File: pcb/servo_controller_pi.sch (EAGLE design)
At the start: 70 parts, among them IC1 PIC18F452, IC2 LM2936MP-5.0, IC3 MAX4173FESA+, IC4 LM2936MP-3.3, IC5 4512D, Q1 10Mhz, Q2 BUZ10

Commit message: Raspberry Pi pcb version
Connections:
- net +3V3: now also C10.1, C11.1, C3.1, C6.1, EXT.1, GY-27.5, IC1.VDD, IC1.VDD@1, IC3.VCC, IC5P.VDD, LED-STRIP.4, R5.2, R6.2, R7.2, SV1.1, SV1.3, SV1.5, SV1.7, SV2.1, SV2.3, SV2.5, SV2.7, VDD.TP; no longer U$3.17-DNC
- net +5V: no longer C10.1, C11.1, C3.1, C6.1, EXT.1, GY-27.5, IC1.VDD, IC1.VDD@1, IC3.VCC, IC5P.VDD, LED-STRIP.4, R5.2, R6.2, R7.2, SV1.1, SV1.3, SV1.5, SV1.7, SV2.1, SV2.3, SV2.5, SV2.7, U$3.4-DNC, VDD.TP
- net LIPO_VOLTAGE: now also IC1.RA5/AN4
- net SERVO_CURRENT: now also IC1.RE0/!RD/AN5
- net VSS: no longer U$3.14-DNC, U$3.20-DNC, U$3.25-DNC, U$3.9-DNC
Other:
- note added: "Sensors"
- moved on the sheet: C10, C7, C8, D4, IC5, IC5P, Q1, RN1, SV1, SV2

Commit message: Schema Pi
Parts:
- removed EXT: (no value), con-lstb:MA03-2
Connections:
- removed net N$16: SJ1.2
- removed net OPTION0: EXT.3
- removed net OPTION1: EXT.5
- removed net OPTION2: EXT.6
- removed net OPTION3: EXT.4
- removed net RX_FROM_ARDUINO: IC1.TX/RC6
- removed net SWITCH0: R6.1, S0.S
- removed net SWITCH1: R5.1, S1.S1
- removed net TX_FROM_ARDUINO: IC1.RX/RC7
- new net RX_PI: IC1.TX/RC6, U$3.10-RX
- new net SO: U$3.23-SPI-SCLK
- new net SW0: R6.1, S0.S, U$3.16-GPIO4
- new net SW1: R5.1, S1.S1, U$3.18-GPIO5
- new net TX_PI: IC1.RX/RC7, U$3.8-TX
- net +3V3: no longer EXT.1, LED-STRIP.4
- net +5V: now also LED-STRIP.4
- net ADDRA: now also U$3.22-GPIO6
- net ADDRB: now also U$3.24-SPI-CE0-N
- net ADDRC: now also U$3.26-SPI-CE1-N
- net DO: now also U$3.19-SPI-MOSI
- net LED0: now also U$3.7-GPIO7
- net LED1: now also U$3.11-GPIO0
- net OUT: now also U$3.12-GPIO1
- net POUT: now also U$3.15-GPIO3
- net SCL: now also U$3.5-SCL0
- net SDA: now also U$3.3-SDA0
- net VSS: no longer EXT.2
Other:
- moved on the sheet: C11, C3, D2, GY-27, IC3, IN-1, IN-2, LED-STRIP, OUT-1, OUT-2, Q2, R5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

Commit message: Raspberry Pi PCB
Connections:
- net UC_RESET: no longer SJ1.1
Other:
- moved on the sheet: SJ1
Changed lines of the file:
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@@
 <instance part="VSS25" gate="G$1" x="38.1" y="200.66"/>
 <instance part="VSS26" gate="G$1" x="157.48" y="180.34"/>
-<instance part="SJ1" gate="1" x="332.74" y="121.92" rot="R90"/>
+<instance part="SJ1" gate="1" x="180.34" y="132.08" rot="R90"/>
 <instance part="C9" gate="G$1" x="86.36" y="220.98"/>
 <instance part="VSS27" gate="G$1" x="86.36" y="200.66"/>
@@
 <pinref part="RESET" gate="G$1" pin="TP"/>
 </segment>
-<segment>
-<pinref part="SJ1" gate="1" pin="1"/>
-<wire x1="332.74" y1="116.84" x2="332.74" y2="114.3" width="0.1524" layer="91"/>
-<junction x="332.74" y="114.3"/>
-<label x="327.66" y="116.84" size="1.778" layer="95"/>
-</segment>
-</net>
+</net>

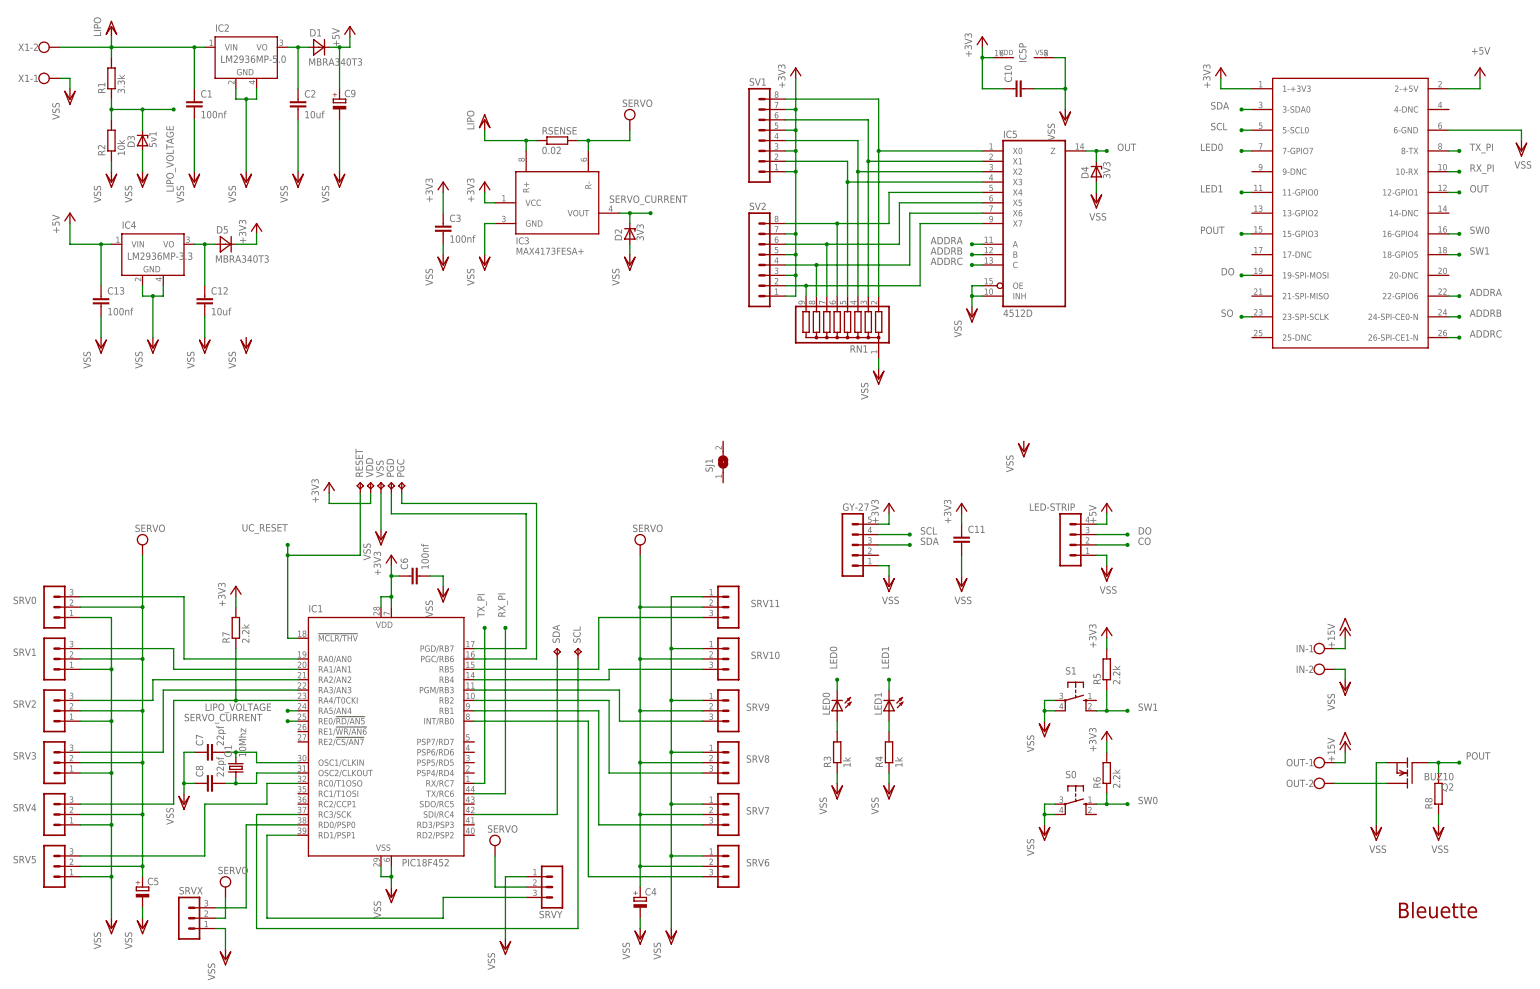
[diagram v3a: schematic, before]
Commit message: Sensor board milling + Raspberry Pi update
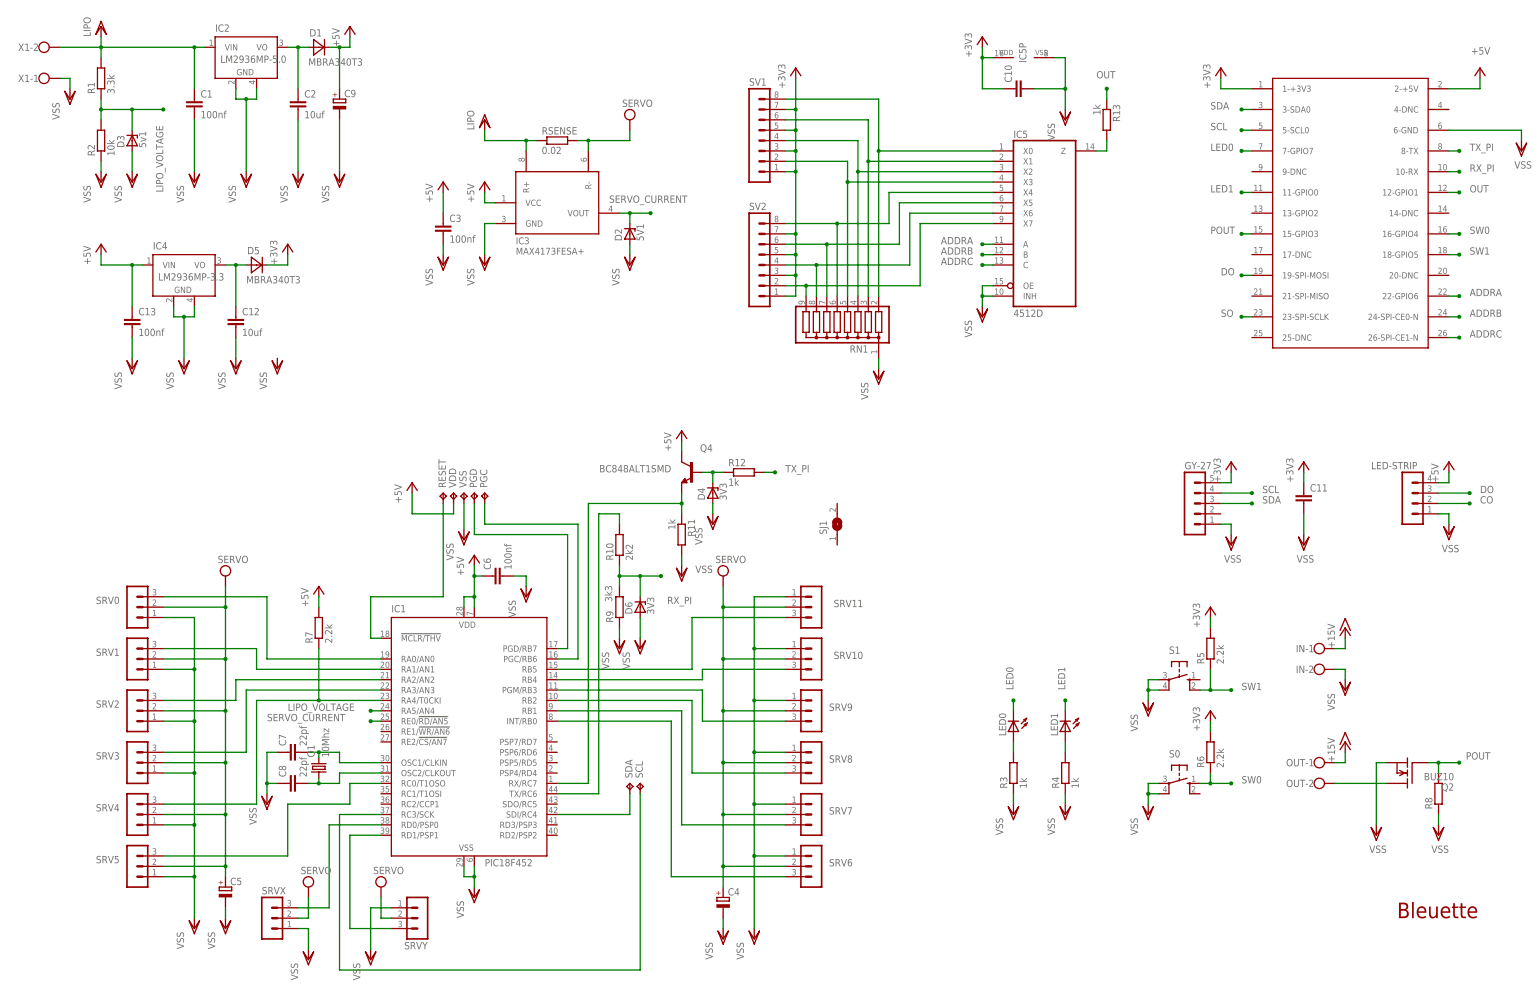
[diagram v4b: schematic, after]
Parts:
- added D6: 3V3, diode:ZENER-DIODESOT23
- added Q4: BC848ALT1SMD, transistor-npn:BC848ALT1SMD
- added R10: 2k2, rcl:R-EU_M0805
- added R11, R12, R13: 1k, rcl:R-EU_M0805
- added R9: 3k3, rcl:R-EU_M0805
- D2: value 3V3 -> 5V1
- R1, R2: device rcl:R-EU_M1206 -> rcl:R-EU_M0805
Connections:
- new net N$15: IC1.RX/RC7, Q4.E, R11.1
- new net N$16: IC1.TX/RC6, R10.2
- new net N$21: D4.C, Q4.B, R12.1
- new net N$37: IC5A.Z, R13.2
- net +3V3: no longer C3.1, C6.1, IC1.VDD, IC1.VDD@1, IC3.VCC, R7.2, VDD.TP
- net +5V: now also C3.1, C6.1, IC1.VDD, IC1.VDD@1, IC3.VCC, Q4.C, R7.2, VDD.TP
- net OUT: now also R13.1; no longer D4.C, IC5A.Z
- net RX_PI: now also D6.C, R10.1, R9.2; no longer IC1.TX/RC6
- net TX_PI: now also R12.2; no longer IC1.RX/RC7
- net VSS: now also D6.A, R11.2, R9.1
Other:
- moved on the sheet: C11, C12, C13, C4, C5, C6, C7, C8, D3, D4, D5, GY-27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

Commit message: RaspPi Board
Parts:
- added IC7: LM358D, linear:LM358D
- C3, C6, C7, C8: device rcl:C-EUC1206 -> rcl:C-EUC0805
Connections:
- net +5V: no longer U$3.2-+5V
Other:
- moved on the sheet: C3, C6, D2, IC3, RSENSE

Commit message: Rapsberry Pi board
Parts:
- removed D4: 3V3, diode:ZENER-DIODESOT23
- removed GY-27: (no value), con-lstb:MA05-1
- removed LED0, LED1: (no value), led:LEDCHIPLED_0805
- removed R3, R4: 1k, rcl:R-EU_M0805
- removed R5, R6: 2.2k, rcl:R-EU_M0805
- removed S0, S1: (no value), switch-omron:10-XX
- added LED2: (no value), led:LEDCHIPLED_0805
- added R14: 1k, rcl:R-EU_M0805
- added SV3: (no value), con-lstb:MA04-2
- added U$4: GY-27, gy-27:GY-27
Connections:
- net DO renamed DI
- removed net CO: LED-STRIP.2
- removed net LED0: LED0.C, U$3.7-GPIO7
- removed net LED1: LED1.C, U$3.11-GPIO0
- removed net N$7: LED0.A, R3.2
- removed net N$8: LED1.A, R4.2
- removed net SO: U$3.23-SPI-SCLK
- removed net SW0: R6.1, S0.S, U$3.16-GPIO4
- removed net SW1: R5.1, S1.S1, U$3.18-GPIO5
- new net N$39: LED2.A, R14.2
- new net OPTION0: SV3.3, U$3.7-GPIO7
- new net OPTION1: SV3.4, U$3.11-GPIO0
- new net OPTION2: SV3.5, U$3.16-GPIO4
- new net OPTION3: SV3.6, U$3.18-GPIO5
- new net SI: LED-STRIP.2, U$3.23-SPI-SCLK
- net +3V3: now also LED2.C, SV3.1, U$4.VCC; no longer GY-27.5, R5.2, R6.2
- net N$21: no longer D4.C
- net SCL: now also SV3.7, U$4.SCL; no longer GY-27.4
- net SDA: now also SV3.8, U$4.SDA; no longer GY-27.3
- net VSS: now also R14.1, SV3.2, U$4.GND; no longer D4.A, GY-27.1, R3.1, R4.1, S0.P, S0.P1, S1.P, S1.P1
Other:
- moved on the sheet: C11, IN-1, IN-2, OUT-1, OUT-2, Q2, R12, R8

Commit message: Bleuette Pi
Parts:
- removed C13: 100nf, rcl:C-EUC1206
- removed C8: 22pf, rcl:C-EUC0805
- removed D1, D5: MBRA340T3, diode:MBRA340T3
- removed IC2: LM2936MP-5.0, national-semiconductor:LM2936MP-3.0
- removed IC7: LM358D, linear:LM358D
- removed IN, OUT, X1: (no value), con-wago-500:W237-102
- removed Q2: BUZ10, transistor-fet:BUZ10
- removed R8: (no value), rcl:R-EU_M0805
- removed SCL, SDA: TPTP20R, testpad:TPTP20R
- removed SV3: (no value), con-lstb:MA04-2
- added C14, C15: (no value), rcl:CPOL-EUA
- added C16: (no value), rcl:CPOL-EUB
- added C17: 100nf, rcl:C-EUC0805
- added IC6: LM386M-1, linear:LM386M-1
- added P5V, PGND, PLIPO: (no value), wirepad:2,54/0,8
- added R15: (no value), pot:TRIM_EU-3223J
- added R3: (no value), rcl:R-EU_M0805
- added SV4: (no value), con-lstb:MA03-1
- added SV5: (no value), con-lstb:MA05-2
- C1: value 100nf -> (none); device rcl:C-EUC1206 -> rcl:CPOL-EUF
- C10, C11: value (none) -> 22pf
- C12: value 10uf -> (none); device rcl:C-EUC1206 -> rcl:C-EUC0805
- C2: value 10uf -> (none); device rcl:C-EUC1206 -> rcl:CPOL-EUF
- C4: value (none) -> 10uf; device rcl:CPOL-EUD -> rcl:C-EUC0805
- C5: value (none) -> 100nf; device rcl:CPOL-EUD -> rcl:C-EUC0805
- C6: value 100nf -> (none)
- C7: value 22pf -> 100nf
- C9: device rcl:CPOL-EUF -> rcl:CPOL-EUD
- renumbered SRV0 to S0, SRV1 to S1, SRV10 to S10, SRV11 to S11, SRV2 to S2, SRV3 to S3, SRV4 to S4, SRV5 to S5, SRV6 to S6, SRV7 to S7, SRV8 to S8, SRV9 to S9, SRVX to SX, SRVY to SY
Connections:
- removed net +15V: IN-1.KL, OUT-1.KL
- removed net N$18: IC1.RC3/SCK, SCL.TP
- removed net N$20: C2.1, D1.A, IC2.VO
- removed net N$36: OUT-2.KL, Q2.D
- removed net N$38: C12.1, D5.A, IC4.VO
- removed net N$9: IC1.SDI/RC4, SDA.TP
- removed net POUT: Q2.G, R8.2, U$3.15-GPIO3
- new net N$40: C15.+, SV4.2
- new net N$41: IC6.+IN, R15.S
- new net N$42: C16.+, IC6.OUT, R3.2
- new net N$43: C17.1, R3.1
- new net N$7: C14.-, C15.-, R15.E
- new net N$8: C14.+, SV4.3
- new net OPTION4: SV5.5, U$3.15-GPIO3
- net +3V3: now also C12.1, C4.1, C6.1, IC4.VO, SV5.9; no longer C10.1, C11.1, D5.C, SV3.1, U$3.1-+3V3
- net +5V: now also C2.+, C5.1, C7.1, IC6.VS, P5V.P, SV5.10, U$3.2-+5V; no longer C13.1, C6.1, C9.+, D1.C
- net N$25: now also C11.2; no longer C8.2
- net N$27: now also C10.2; no longer C7.2
- net OPTION0: now also SV5.1; no longer SV3.3
- net OPTION1: now also SV5.2; no longer SV3.4
- net OPTION2: now also SV5.3; no longer SV3.5
- net OPTION3: now also SV5.4; no longer SV3.6
- net SCL: now also SV5.8; no longer SV3.7
- net SDA: now also SV5.6; no longer SV3.8
- net VDD: now also C1.+, PLIPO.P; no longer C1.1, IC2.VIN, X1-2.KL
- net VEE: now also C9.+; no longer C4.+, C5.+
- net VSS: now also C1.-, C10.1, C11.1, C17.2, C2.-, C4.2, C5.2, C7.2, IC6.-IN, IC6.GND, PGND.P, R15.A, SV4.1, SV5.7; no longer C1.2, C10.2, C11.2, C13.2, C2.2, C4.-, C5.-, C7.1, C8.1, IC2.GND@1, IC2.GND@2, IN-2.KL, Q2.S, R8.1, SV3.2, X1-1.KL
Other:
- moved on the sheet: C10, C11, C12, C3, C6, C7, C9, D2, D3, IC3, LED-STRIP, R1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

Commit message: BleuettePi
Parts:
- removed SJ1: (no value), jumper:SJ
- added C8: (no value), rcl:CPOL-EUA
- added HP+, HP-: (no value), wirepad:2,54/0,8
- renumbered LED2 to PWR
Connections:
- new net N$9: C16.-, HP+.P
- net +5V: now also C8.+
- net VSS: now also C8.-, HP-.P
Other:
- moved on the sheet: C14, C15, C16, C17, IC6, LED-STRIP, R15, R3, SV4, SV5
